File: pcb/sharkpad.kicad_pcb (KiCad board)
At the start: 2 copper layers, 89.8 x 19.3 mm, 7 parts, among them SW1 SW_Push, SW2 SW_Push, SW3 SW_Push, SW4 SW_Push, U1 MOUDLE-SEEEDUINO-XIAO

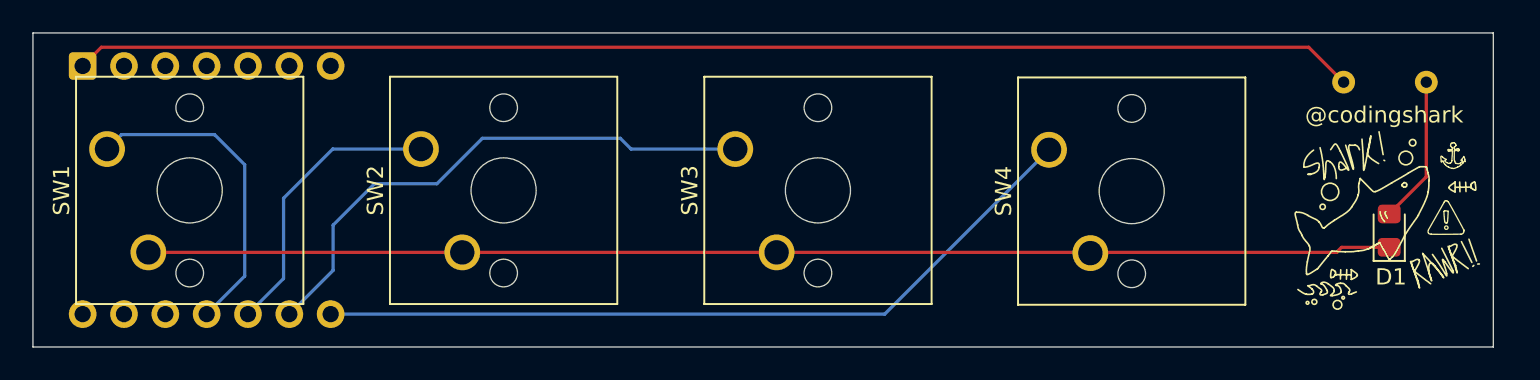
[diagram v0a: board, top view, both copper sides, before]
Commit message: add assembled version and update pcb
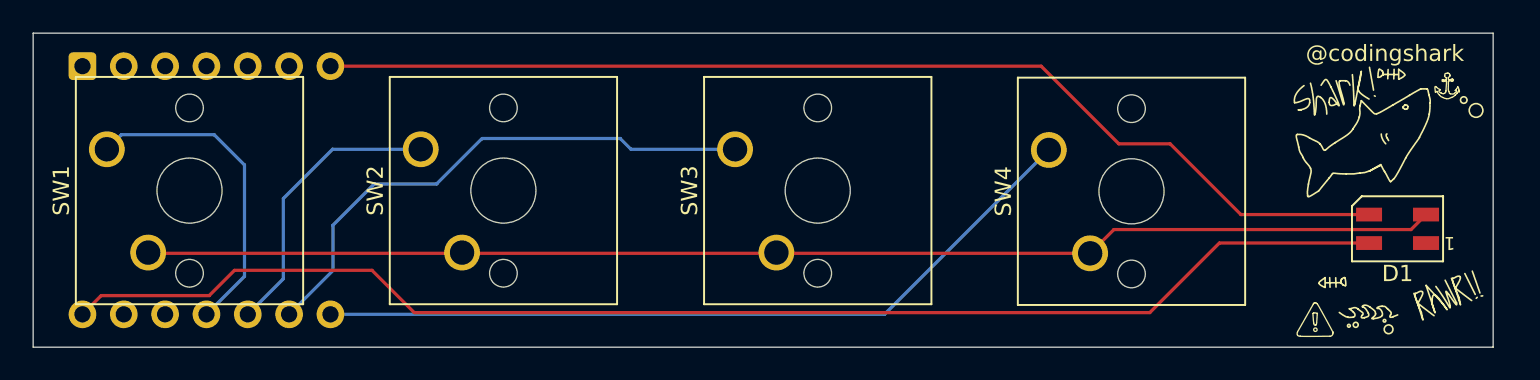
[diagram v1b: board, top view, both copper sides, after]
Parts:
- removed R1: R, Resistor_THT:R_Axial_DIN0204_L3.6mm_D1.6mm_P5.08mm_Horizontal
- D1: value LED -> SK6812MINI; footprint LED_SMD:LED_0805_2012Metric_Pad1.15x1.40mm_HandSolder -> LED_SMD:LED_SK6812MINI_PLCC4_3.5x3.5mm_P1.75mm
- moved D1 0.52 mm to (166.0, 100.1), turned to 180 degrees
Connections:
- D1 pad 1: GND -> unconnected-(D1-DOUT-Pad1)
- D1 pad 2: Net-(D1-A) -> GND
- U1 pad 1: Net-(U1-PA02_A0_D0) -> unconnected-(U1-PA02_A0_D0-Pad1)
- U1 pad 14: unconnected-(U1-5V-Pad14) -> Net-(D1-VDD)
- U1 pad 7: unconnected-(U1-PB08_A6_D6_TX-Pad7) -> Net-(D1-DIN)
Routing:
- net Net-(D1-VDD): track 0.00 -> 83.0 mm
- net Net-(U1-PA02_A0_D0): track 78.9 -> 0.00 mm
- net Net-(D1-DIN): track 0.00 -> 67.6 mm
- net Net-(D1-A): track 9.04 -> 0.00 mm
- net GND: track 77.0 -> 79.5 mm
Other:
- board size 89.8 x 19.3 mm -> 89.7 x 19.3 mm
